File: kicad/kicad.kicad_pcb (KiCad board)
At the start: 2 copper layers, 70 x 70 mm, 16 parts, among them SW1 SW_Push, U2 ATtiny85-20P

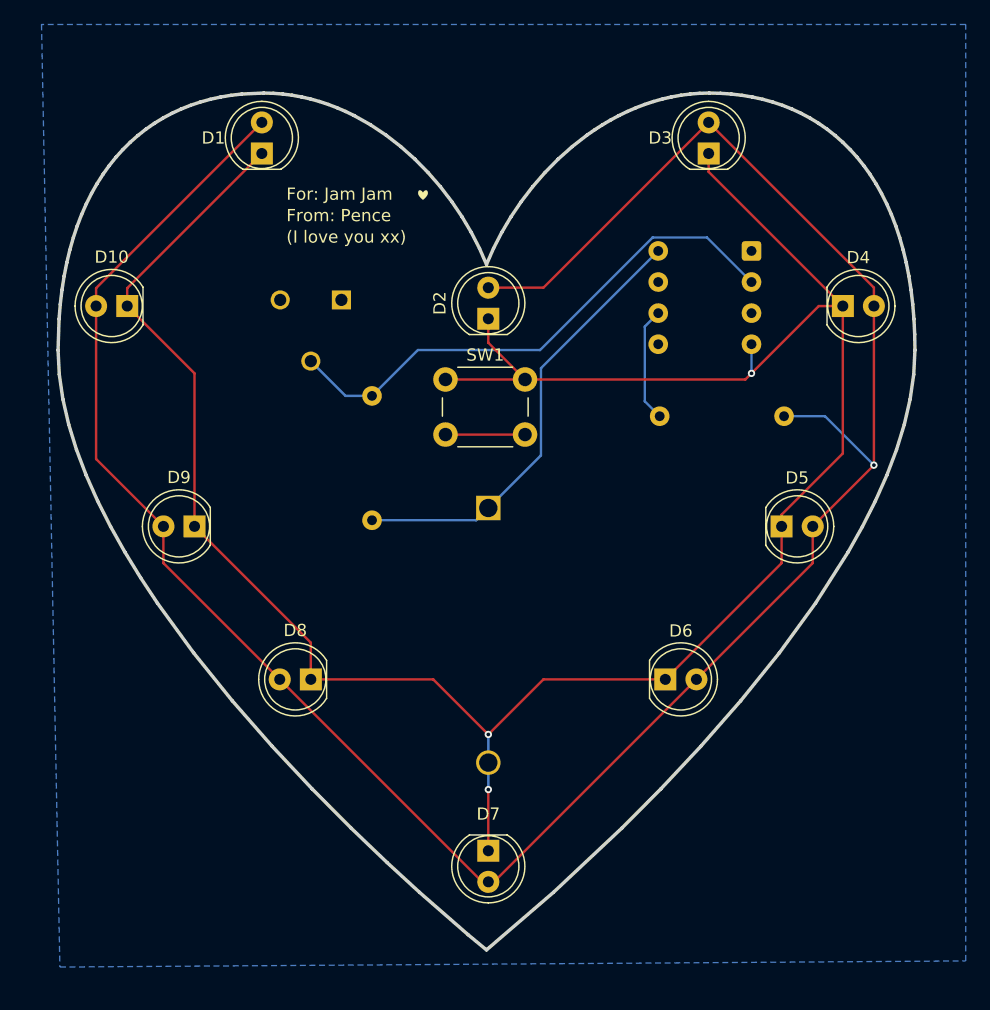
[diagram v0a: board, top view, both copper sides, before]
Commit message: Session #3: Smooth PWM breathing fade + gamma correction
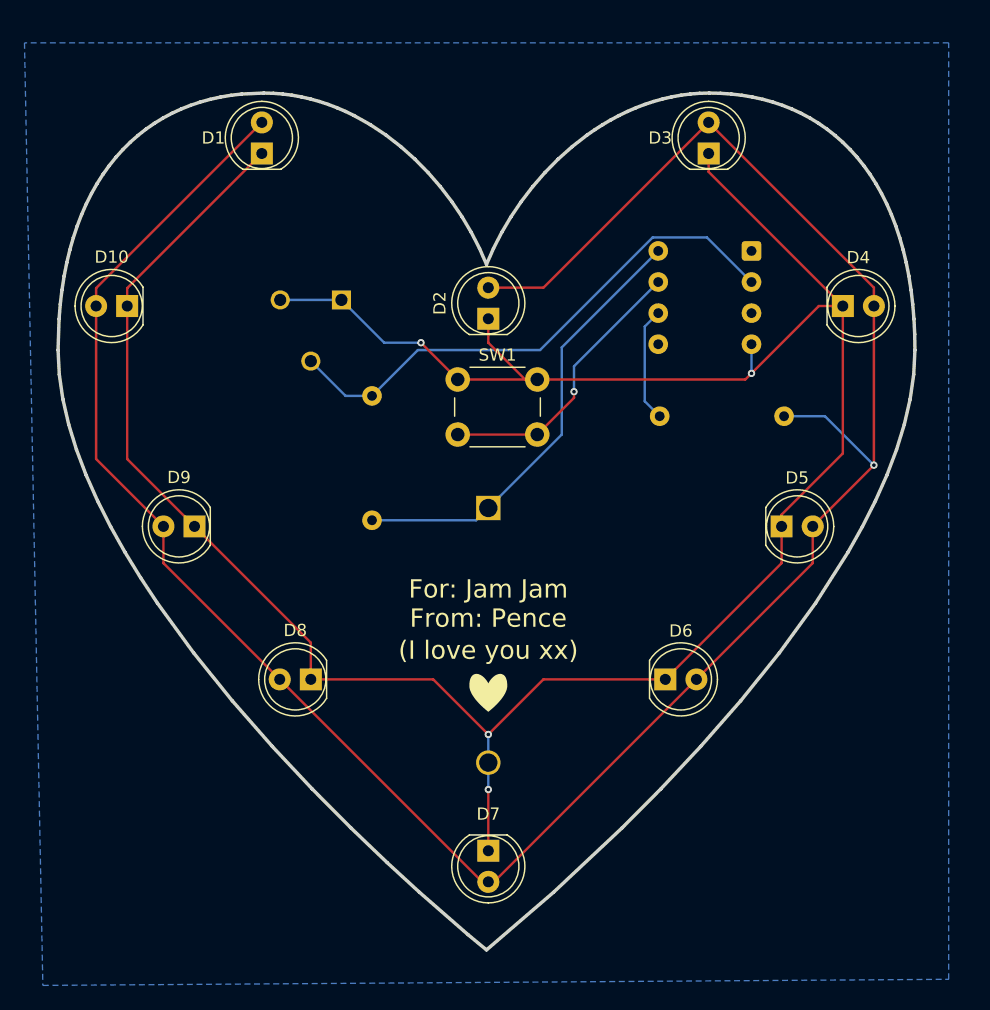
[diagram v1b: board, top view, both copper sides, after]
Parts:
- moved SW1 1.00 mm to (138.5, 89.0)
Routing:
- net GND: track 193.0 -> 210.1 mm, vias 3 -> 4
- net Net-(U2-PB2): track 6.50 -> 23.1 mm, vias 0 -> 1
- net Net-(U2-XTAL1/PB3): track 44.0 -> 44.5 mm

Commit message: Session #4: Trimpot brightness control, README update
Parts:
- removed R2: 10k, Resistor_THT:R_Axial_DIN0207_L6.3mm_D2.5mm_P10.16mm_Horizontal
- added SW2: SW_SPDT, Button_Switch_THT:SW_Slide-03_Wuerth-WS-SLTV_10x2.5x6.4_P2.54mm, B.Cu at (0.00, 0.00)
- BT2: value Battery_Cell -> Battery
- moved D5 193.4 mm to (0.00, 0.00)
- moved D6 192.5 mm to (0.00, 0.00)
- moved D7 190.1 mm to (0.00, 0.00), turned to 0 degrees
- moved D4 189.1 mm to (0.00, 0.00)
- moved U2 180.5 mm to (0.00, 0.00), turned to 0 degrees
- moved R1 180.2 mm to (0.00, 0.00)
- moved D3 173.9 mm to (0.00, 0.00), turned to 0 degrees
- moved BT2 172.6 mm to (0.00, 0.00), turned to 0 degrees
- moved D8 170.0 mm to (0.00, 0.00), turned to 0 degrees
- moved SW1 164.6 mm to (0.00, 0.00)
- moved D2 164.1 mm to (0.00, 0.00), turned to 0 degrees
- moved D9 154.6 mm to (0.00, 0.00), turned to 0 degrees
- moved RV1 153.1 mm to (0.00, 0.00), turned to 0 degrees
- moved D1 141.4 mm to (0.00, 0.00), turned to 0 degrees
- moved D10 139.0 mm to (0.00, 0.00), turned to 0 degrees
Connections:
- RV1 pad 3: GND -> Net-(SW2-A)
- U2 pad 8: Net-(BT2-+) -> Net-(SW2-A)
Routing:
- net Net-(SW2-A): track 0.00 -> 55.7 mm
- net Net-(BT2-+): track 36.7 -> 14.2 mm
- net GND: track 210.1 -> 205.1 mm
- net Net-(U2-XTAL1/PB3): track 44.5 -> 42.2 mm
- net Net-(D1-A): track 194.8 -> 196.5 mm
- net Net-(U2-PB1): track 9.38 -> 8.49 mm
